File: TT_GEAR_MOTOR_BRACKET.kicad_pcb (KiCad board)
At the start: 2 copper layers, 41.8 x 22.5 mm, 5 parts

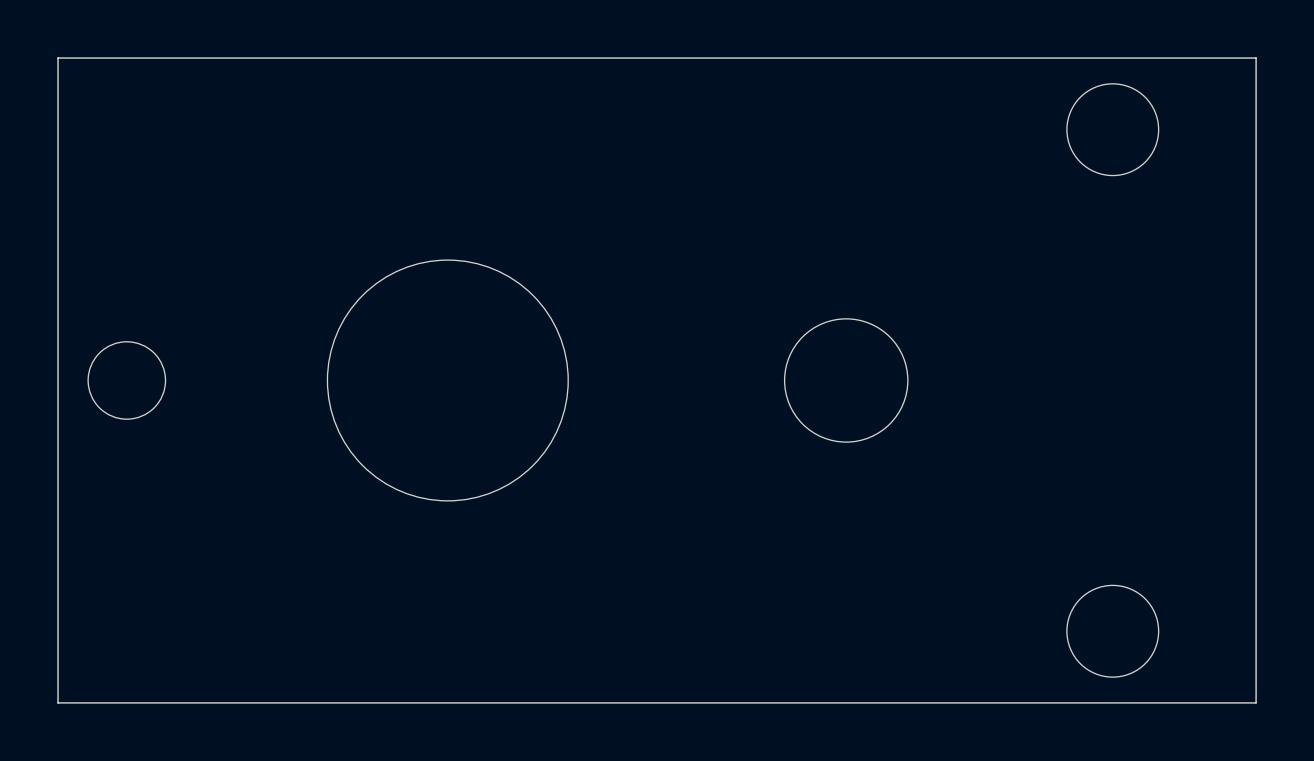
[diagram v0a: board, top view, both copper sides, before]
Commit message: corrected axle measurement
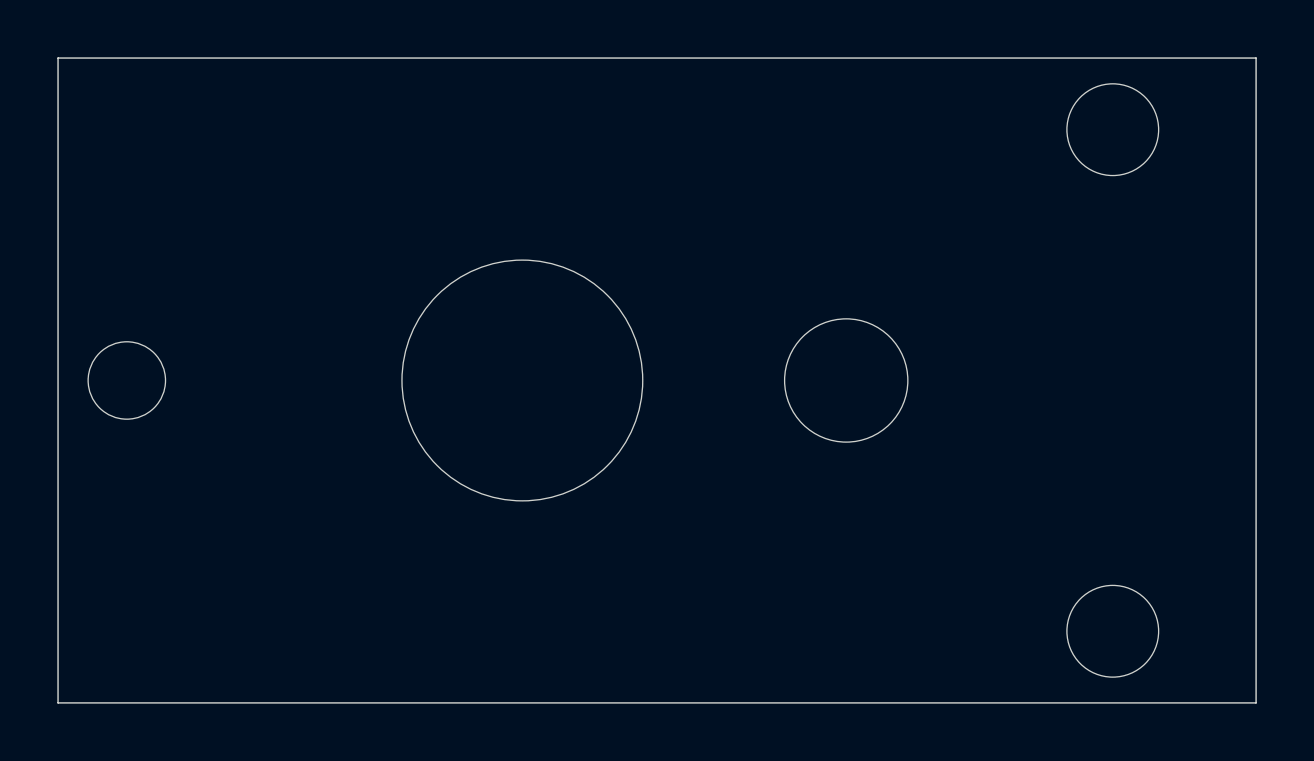
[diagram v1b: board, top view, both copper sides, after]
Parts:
- moved REF** 2.60 mm to (66.2, 61.2)
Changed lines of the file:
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@@
   )
   (module MountingHole:MountingHole_8.4mm_M8 (layer F.Cu)
-    (at 63.6 61.25)
+    (at 66.2 61.25)
     (descr "Mounting Hole 8.4mm, no annular, M8")
     (tags "mounting hole 8.4mm no annular m8")
